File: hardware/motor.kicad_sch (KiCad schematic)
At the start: 16 parts, among them J5 Conn_01x02_Socket, J6 Conn_01x02_Socket, J7 Conn_01x02_Socket, J8 Conn_01x02_Socket, Q1 AO3400A, Q2 AO3400A, Q3 AO3400A, Q4 AO3400A

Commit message: feat(kicad): Cleared ERC errors and assigned footprints for all parts
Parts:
- D1, D2, D3, D4: footprint (none) -> Diode_SMD:D_MicroSMP_LargeCathode
- R12, R13, R14, R15: footprint (none) -> Resistor_SMD:R_0402_1005Metric
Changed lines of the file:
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@@
 			)
 		)
-		(property "Footprint" ""
+		(property "Footprint" "Resistor_SMD:R_0402_1005Metric"
 			(at 146.812 74.93 90)
 			(hide yes)
@@
 			)
 		)
-		(property "Footprint" ""
+		(property "Footprint" "Diode_SMD:D_MicroSMP_LargeCathode"
 			(at 185.42 58.42 0)
 			(hide yes)
@@
 			)
 		)
-		(property "Footprint" ""
+		(property "Footprint" "Diode_SMD:D_MicroSMP_LargeCathode"
 			(at 128.27 58.42 0)
 			(hide yes)
@@
 			)
 		)
-		(property "Footprint" ""
+		(property "Footprint" "Diode_SMD:D_MicroSMP_LargeCathode"
 			(at 100.33 58.42 0)
 			(hide yes)
@@
 			)
 		)
-		(property "Footprint" ""
+		(property "Footprint" "Resistor_SMD:R_0402_1005Metric"
 			(at 118.872 74.93 90)
 			(hide yes)
@@
 			)
 		)
-		(property "Footprint" ""
+		(property "Footprint" "Diode_SMD:D_MicroSMP_LargeCathode"
 			(at 156.21 58.42 0)
 			(hide yes)
@@
 			)
 		)
-		(property "Footprint" ""
+		(property "Footprint" "Resistor_SMD:R_0402_1005Metric"
 			(at 90.932 74.93 90)
 			(hide yes)
@@
 			)
 		)
-		(property "Footprint" ""
+		(property "Footprint" "Resistor_SMD:R_0402_1005Metric"
 			(at 176.022 74.93 90)
 			(hide yes)

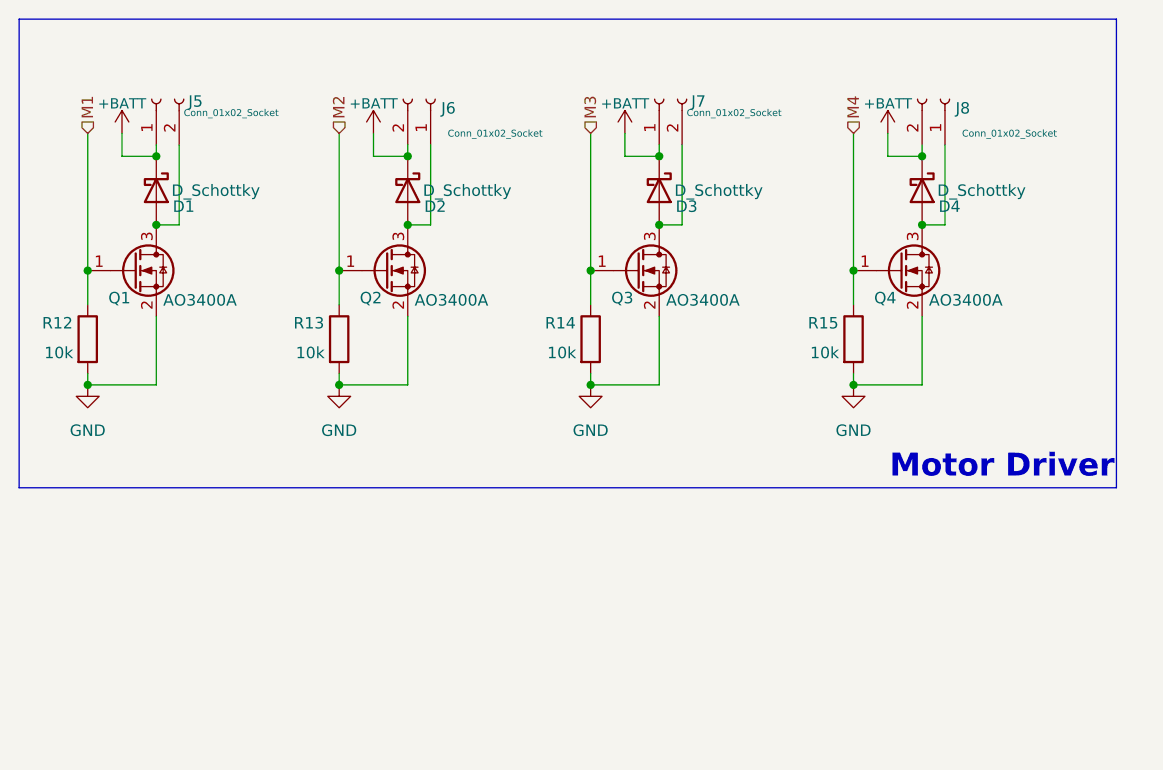
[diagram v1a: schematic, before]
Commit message: feat (kicad): Added Motor driving application notes
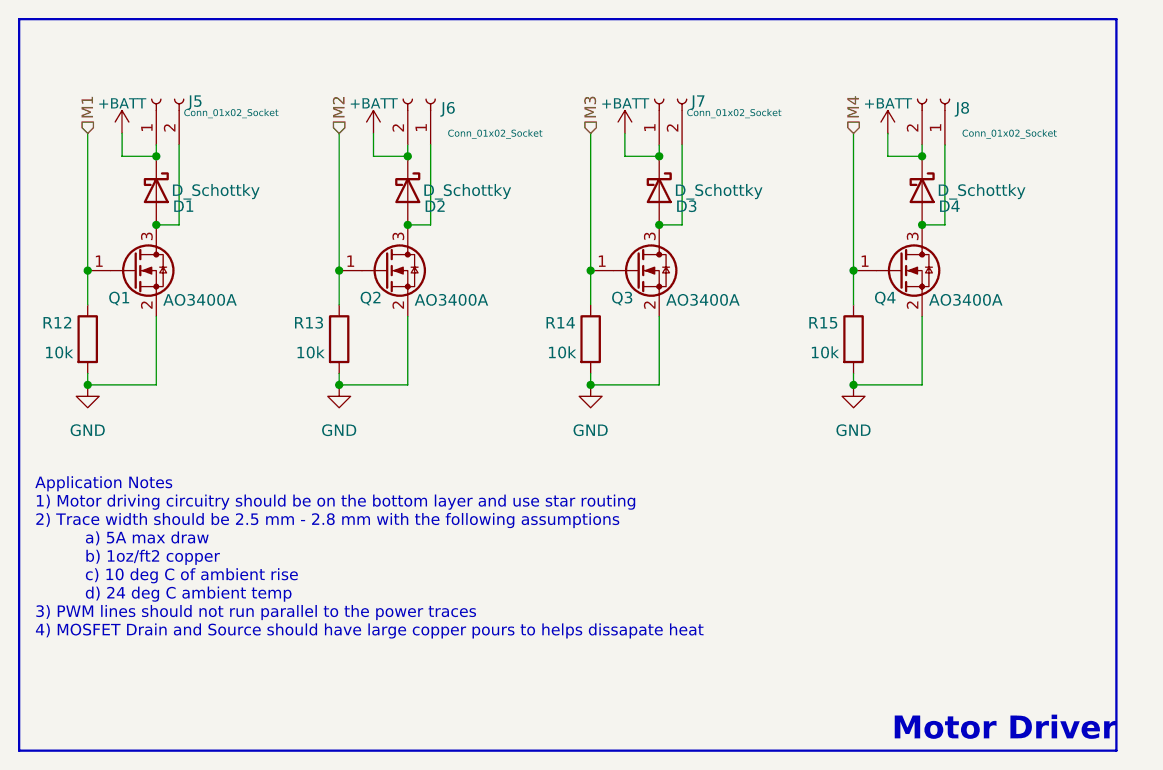
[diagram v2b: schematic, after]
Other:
- note added: "Application Notes 1) Motor driving circuitry should be on the bottom layer and use star routing 2) Trace width should be 2.5 mm - 2.8 mm with the following assumptions a) 5A max draw b) 1oz/ft2 copper c) 10 deg C of ambient rise d) 24 deg C ambient temp 3) PWM lines should not run parallel to the power traces 4) MOSFET Drain and Source should have large copper pours to helps dissapate heat"
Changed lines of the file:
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@@
 	(rectangle
 		(start 85.09 39.37)
-		(end 207.01 91.44)
+		(end 207.01 120.65)
 		(stroke
-			(width 0.0762)
+			(width 0.254)
 			(type solid)
 		)
@@
 		)
 	)
+	(text "Application Notes\n1) Motor driving circuitry should be on the bottom layer and use star routing\n2) Trace width should be 2.5 mm - 2.8 mm with the following assumptions\n          a) 5A max draw\n          b) 1oz/ft2 copper\n          c) 10 deg C of ambient rise\n          d) 24 deg C ambient temp\n3) PWM lines should not run parallel to the power traces\n4) MOSFET Drain and Source should have large copper pours to helps dissapate heat"
+		(exclude_from_sim no)
+		(at 86.868 99.314 0)
+		(effects
+			(font
+				(size 1.27 1.27)
+			)
+			(justify left)
+		)
+	)
 	(text "Motor Driver\n"
 		(exclude_from_sim no)
-		(at 194.31 89.154 0)
+		(at 194.564 118.364 0)
 		(effects
 			(font

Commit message: feat(kicad): Initial pcb layout
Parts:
- J5, J6, J7, J8: footprint (none) -> Connector_JST:JST_ZH_B2B-ZR_1x02_P1.50mm_Vertical
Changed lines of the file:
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@@
 			)
 		)
-		(property "Footprint" ""
+		(property "Footprint" "Connector_JST:JST_ZH_B2B-ZR_1x02_P1.50mm_Vertical"
 			(at 130.81 48.26 0)
 			(hide yes)
@@
 			)
 		)
-		(property "Footprint" ""
+		(property "Footprint" "Connector_JST:JST_ZH_B2B-ZR_1x02_P1.50mm_Vertical"
 			(at 156.21 48.26 0)
 			(hide yes)
@@
 			)
 		)
-		(property "Footprint" ""
+		(property "Footprint" "Connector_JST:JST_ZH_B2B-ZR_1x02_P1.50mm_Vertical"
 			(at 187.96 48.26 0)
 			(hide yes)
@@
 			)
 		)
-		(property "Footprint" ""
+		(property "Footprint" "Connector_JST:JST_ZH_B2B-ZR_1x02_P1.50mm_Vertical"
 			(at 100.33 48.26 0)
 			(hide yes)

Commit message: feat(kicad): Added step files for missing parts
changed flyback diode to SMA part with 5A max

Redid initial layout
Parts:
- D1, D2, D3, D4: value D_Schottky -> D_Schottky (C22452); footprint Diode_SMD:D_MicroSMP_LargeCathode -> Diode_SMD:D_SMA
- J5, J6, J7, J8: footprint Connector_JST:JST_ZH_B2B-ZR_1x02_P1.50mm_Vertical -> MotorJST:JST_S2B-ZR-3.4_LF__SN_
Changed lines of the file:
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@@
 			)
 		)
-		(property "Footprint" "Connector_JST:JST_ZH_B2B-ZR_1x02_P1.50mm_Vertical"
+		(property "Footprint" "MotorJST:JST_S2B-ZR-3.4_LF__SN_"
 			(at 130.81 48.26 0)
 			(hide yes)
@@
 			)
 		)
-		(property "Value" "D_Schottky"
+		(property "Value" "D_Schottky (C22452)"
 			(at 192.024 58.42 90)
 			(show_name no)
@@
 			)
 		)
-		(property "Footprint" "Diode_SMD:D_MicroSMP_LargeCathode"
+		(property "Footprint" "Diode_SMD:D_SMA"
 			(at 185.42 58.42 0)
 			(hide yes)
@@
 			)
 		)
-		(property "Value" "D_Schottky"
-			(at 134.874 58.42 90)
-			(show_name no)
-			(do_not_autoplace no)
-			(effects
-				(font
-					(size 1.27 1.27)
-				)
-			)
-		)
-		(property "Footprint" "Diode_SMD:D_MicroSMP_LargeCathode"
+		(property "Value" "D_Schottky (C22452)"
+			(at 134.874 57.658 90)
+			(show_name no)
+			(do_not_autoplace no)
+			(effects
+				(font
+					(size 1.27 1.27)
+				)
+			)
+		)
+		(property "Footprint" "Diode_SMD:D_SMA"
 			(at 128.27 58.42 0)
 			(hide yes)
@@
 			)
 		)
-		(property "Footprint" "Connector_JST:JST_ZH_B2B-ZR_1x02_P1.50mm_Vertical"
+		(property "Footprint" "MotorJST:JST_S2B-ZR-3.4_LF__SN_"
 			(at 156.21 48.26 0)
 			(hide yes)
@@
 		(dnp no)
 		(property "Reference" "D1"
-			(at 103.378 60.198 90)
-			(show_name no)
-			(do_not_autoplace no)
-			(effects
-				(font
-					(size 1.27 1.27)
-				)
-			)
-		)
-		(property "Value" "D_Schottky"
-			(at 106.934 58.42 90)
-			(show_name no)
-			(do_not_autoplace no)
-			(effects
-				(font
-					(size 1.27 1.27)
-				)
-			)
-		)
-		(property "Footprint" "Diode_SMD:D_MicroSMP_LargeCathode"
+			(at 104.394 61.214 90)
+			(show_name no)
+			(do_not_autoplace no)
+			(effects
+				(font
+					(size 1.27 1.27)
+				)
+			)
+		)
+		(property "Value" "D_Schottky (C22452)"
+			(at 105.156 60.706 90)
+			(show_name no)
+			(do_not_autoplace no)
+			(effects
+				(font
+					(size 1.27 1.27)
+				)
+			)
+		)
+		(property "Footprint" "Diode_SMD:D_SMA"
 			(at 100.33 58.42 0)
 			(hide yes)
@@
 			)
 		)
-		(property "Footprint" "Connector_JST:JST_ZH_B2B-ZR_1x02_P1.50mm_Vertical"
+		(property "Footprint" "MotorJST:JST_S2B-ZR-3.4_LF__SN_"
 			(at 187.96 48.26 0)
 			(hide yes)
@@
 			)
 		)
-		(property "Value" "D_Schottky"
-			(at 162.814 58.42 90)
-			(show_name no)
-			(do_not_autoplace no)
-			(effects
-				(font
-					(size 1.27 1.27)
-				)
-			)
-		)
-		(property "Footprint" "Diode_SMD:D_MicroSMP_LargeCathode"
+		(property "Value" "D_Schottky (C22452)"
+			(at 162.814 57.15 90)
+			(show_name no)
+			(do_not_autoplace no)
+			(effects
+				(font
+					(size 1.27 1.27)
+				)
+			)
+		)
+		(property "Footprint" "Diode_SMD:D_SMA"
 			(at 156.21 58.42 0)
 			(hide yes)
@@
 			)
 		)
-		(property "Footprint" "Connector_JST:JST_ZH_B2B-ZR_1x02_P1.50mm_Vertical"
+		(property "Footprint" "MotorJST:JST_S2B-ZR-3.4_LF__SN_"
 			(at 100.33 48.26 0)
 			(hide yes)

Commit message: feat(kicad): Routing complete, assigning jlc components to each footprint
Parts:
- D1, D2, D3, D4: LCSC (none) -> C22452
- J5, J6, J7, J8: LCSC (none) -> C160729
- Q1, Q2, Q3, Q4: LCSC (none) -> C20917
- R12, R13, R14, R15: value 10k -> 4k7; LCSC (none) -> C25900
